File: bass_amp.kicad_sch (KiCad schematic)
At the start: 12 parts, among them Q1 BC547, Q2 BC547

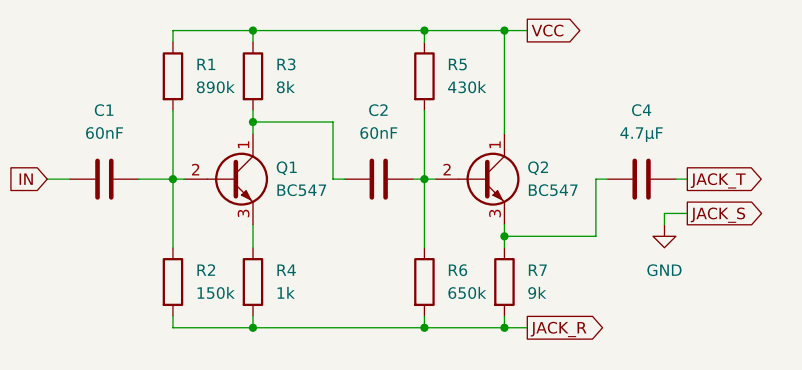
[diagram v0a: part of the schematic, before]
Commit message: Add a potentiometer to change the value of gain
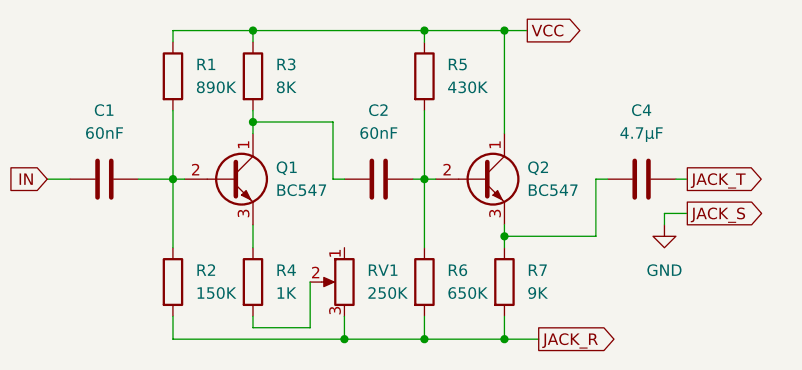
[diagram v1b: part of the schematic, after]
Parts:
- added RV1: 250K, symbol Device:R_Potentiometer
- R1: value 890k -> 890K
- R2: value 150k -> 150K
- R3: value 8k -> 8K
- R4: value 1k -> 1K
- R5: value 430k -> 430K
- R6: value 650k -> 650K
- R7: value 9k -> 9K
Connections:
- net JACK_R: now also RV1.3; no longer R4.2
- new net: R4.2, RV1.2
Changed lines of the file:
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@@
 	(paper "A4")
-	(junction
-		(at 106.68 91.44)
-		(diameter 0)
-		(color 0 0 0 0)
-	)
 	(junction
 		(at 78.74 58.42)
@@
 	)
 	(junction
-		(at 97.79 74.93)
+		(at 97.79 92.71)
 		(diameter 0)
 		(color 0 0 0 0)
 	)
 	(junction
-		(at 97.79 91.44)
+		(at 97.79 74.93)
 		(diameter 0)
 		(color 0 0 0 0)
@@
 	)
 	(junction
-		(at 69.85 74.93)
+		(at 106.68 92.71)
 		(diameter 0)
 		(color 0 0 0 0)
 	)
 	(junction
-		(at 78.74 91.44)
+		(at 69.85 74.93)
 		(diameter 0)
 		(color 0 0 0 0)
@@
 	)
 	(junction
+		(at 88.9 92.71)
+		(diameter 0)
+		(color 0 0 0 0)
+	)
+	(junction
 		(at 106.68 81.28)
 		(diameter 0)
@@
 	(wire
 		(pts
-			(xy 78.74 91.44) (xy 97.79 91.44)
-		)
-		(stroke
-			(width 0)
-			(type default)
-		)
-	)
-	(wire
-		(pts
-			(xy 106.68 90.17) (xy 106.68 91.44)
-		)
-		(stroke
-			(width 0)
-			(type default)
-		)
-	)
-	(wire
-		(pts
-			(xy 97.79 91.44) (xy 106.68 91.44)
+			(xy 85.09 86.36) (xy 85.09 91.44)
 		)
 		(stroke
@@
 	(wire
 		(pts
+			(xy 78.74 91.44) (xy 85.09 91.44)
+		)
+		(stroke
+			(width 0)
+			(type default)
+		)
+	)
+	(wire
+		(pts
 			(xy 127 78.74) (xy 124.46 78.74)
 		)
@@
 	(wire
 		(pts
-			(xy 69.85 91.44) (xy 78.74 91.44)
+			(xy 69.85 92.71) (xy 88.9 92.71)
 		)
 		(stroke
@@
 	(wire
 		(pts
+			(xy 97.79 92.71) (xy 106.68 92.71)
+		)
+		(stroke
+			(width 0)
+			(type default)
+		)
+	)
+	(wire
+		(pts
 			(xy 106.68 81.28) (xy 116.84 81.28)
 		)
@@
 	(wire
 		(pts
-			(xy 106.68 91.44) (xy 109.22 91.44)
+			(xy 78.74 90.17) (xy 78.74 91.44)
+		)
+		(stroke
+			(width 0)
+			(type default)
+		)
+	)
+	(wire
+		(pts
+			(xy 106.68 92.71) (xy 110.49 92.71)
 		)
 		(stroke
@@
 	(wire
 		(pts
-			(xy 78.74 90.17) (xy 78.74 91.44)
-		)
-		(stroke
-			(width 0)
-			(type default)
-		)
-	)
-	(wire
-		(pts
 			(xy 124.46 78.74) (xy 124.46 80.01)
 		)
@@
 	(wire
 		(pts
-			(xy 97.79 90.17) (xy 97.79 91.44)
-		)
-		(stroke
-			(width 0)
-			(type default)
-		)
-	)
-	(wire
-		(pts
 			(xy 97.79 59.69) (xy 97.79 58.42)
 		)
@@
 	(wire
 		(pts
+			(xy 88.9 92.71) (xy 97.79 92.71)
+		)
+		(stroke
+			(width 0)
+			(type default)
+		)
+	)
+	(wire
+		(pts
+			(xy 97.79 90.17) (xy 97.79 92.71)
+		)
+		(stroke
+			(width 0)
+			(type default)
+		)
+	)
+	(wire
+		(pts
 			(xy 97.79 67.31) (xy 97.79 74.93)
 		)
@@
 	(wire
 		(pts
-			(xy 69.85 90.17) (xy 69.85 91.44)
+			(xy 69.85 90.17) (xy 69.85 92.71)
 		)
 		(stroke
@@
 	(wire
 		(pts
+			(xy 106.68 90.17) (xy 106.68 92.71)
+		)
+		(stroke
+			(width 0)
+			(type default)
+		)
+	)
+	(wire
+		(pts
 			(xy 69.85 59.69) (xy 69.85 58.42)
+		)
+		(stroke
+			(width 0)
+			(type default)
+		)
+	)
+	(wire
+		(pts
+			(xy 88.9 90.17) (xy 88.9 92.71)
 		)
 		(stroke
@@
 	(global_label "JACK_R"
 		(shape output)
-		(at 109.22 91.44 0)
+		(at 110.49 92.71 0)
 		(fields_autoplaced yes)
 		(effects
@@
 		)
 		(property "Intersheetrefs" "${INTERSHEET_REFS}"
-			(at 119.039 91.44 0)
+			(at 120.309 92.71 0)
 			(effects
 				(font
@@
 			)
 		)
-		(property "Value" "430k"
+		(property "Value" "430K"
 			(at 100.33 64.7699 0)
 			(effects
@@
 			)
 		)
-		(property "Value" "150k"
+		(property "Value" "150K"
 			(at 72.39 87.6299 0)
 			(effects
@@
 				(path "/03e06cc7-32db-4918-be19-a630bf77c00d"
 					(reference "R2")
+					(unit 1)
+				)
+			)
+		)
+	)
+	(symbol
+		(lib_id "Device:R_Potentiometer")
+		(at 88.9 86.36 0)
+		(mirror y)
+		(unit 1)
+		(exclude_from_sim no)
+		(in_bom yes)
+		(on_board yes)
+		(dnp no)
+		(property "Reference" "RV1"
+			(at 91.44 85.0899 0)
+			(effects
+				(font
+					(size 1.27 1.27)
+				)
+				(justify right)
+			)
+		)
+		(property "Value" "250K"
+			(at 91.44 87.6299 0)
+			(effects
+				(font
+					(size 1.27 1.27)
+				)
+				(justify right)
+			)
+		)
+		(property "Footprint" ""
+			(at 88.9 86.36 0)
+			(effects
+				(font
+					(size 1.27 1.27)
+				)
+				(hide yes)
+			)
+		)
+		(property "Datasheet" "~"
+			(at 88.9 86.36 0)
+			(effects
+				(font
+					(size 1.27 1.27)
+				)
+				(hide yes)
+			)
+		)
+		(property "Description" "Potentiometer"
+			(at 88.9 86.36 0)
+			(effects
+				(font
+					(size 1.27 1.27)
+				)
+				(hide yes)
+			)
+		)
+		(pin "1"
+		)
+		(pin "3"
+		)
+		(pin "2"
+		)
+		(instances
+			(project ""
+				(path "/03e06cc7-32db-4918-be19-a630bf77c00d"
+					(reference "RV1")
 					(unit 1)
 				)
@@
 			)
 		)
-		(property "Value" "9k"
+		(property "Value" "9K"
 			(at 109.22 87.6299 0)
 			(effects
@@
 			)
 		)
-		(property "Value" "8k"
+		(property "Value" "8K"
 			(at 81.28 64.7699 0)
 			(effects
@@
 			)
 		)
-		(property "Value" "650k"
+		(property "Value" "650K"
 			(at 100.33 87.6299 0)
 			(effects
@@
 			)
 		)
-		(property "Value" "890k"
+		(property "Value" "890K"
 			(at 72.39 64.7699 0)
 			(effects
@@
 			)
 		)
-		(property "Value" "1k"
+		(property "Value" "1K"
 			(at 81.28 87.6299 0)
 			(effects

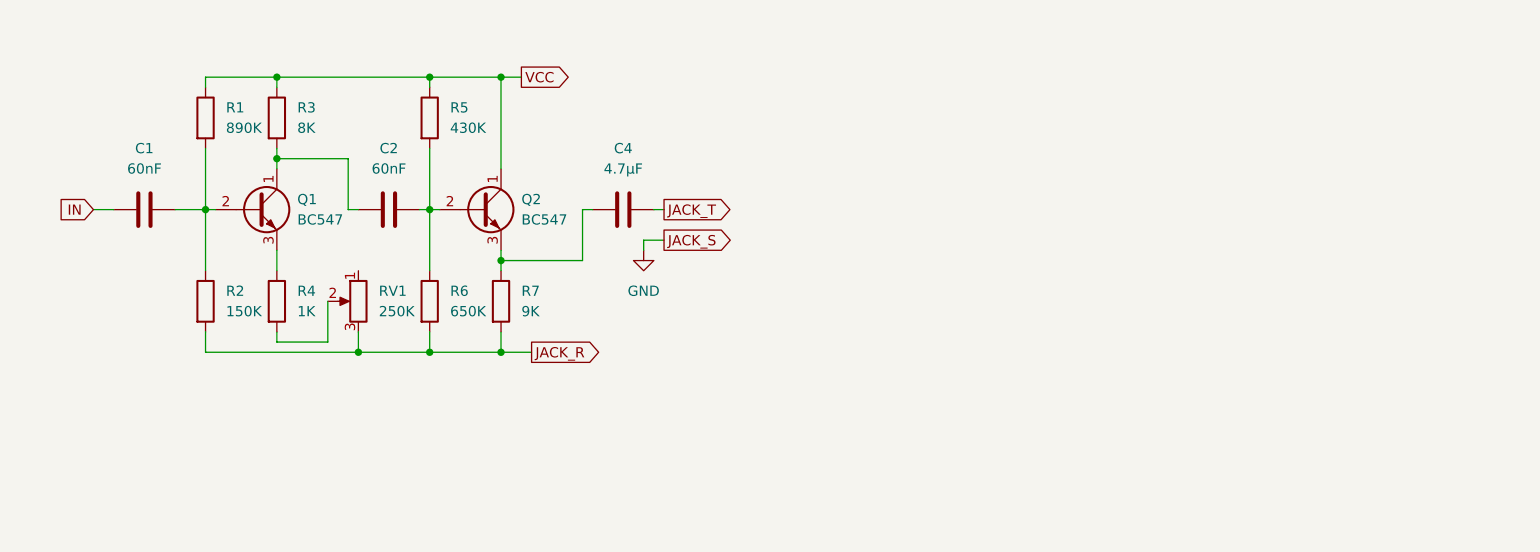
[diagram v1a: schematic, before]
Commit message: Add a bypass circuit
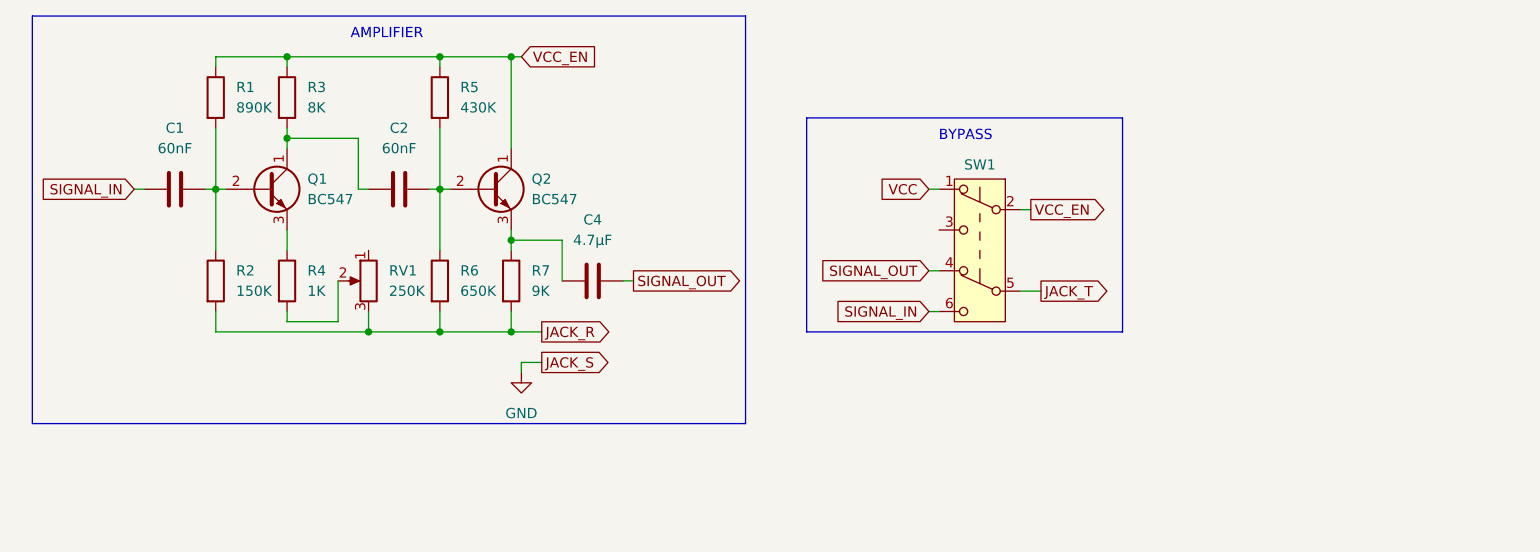
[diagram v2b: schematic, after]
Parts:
- added SW1: SW_Push_DPDT, symbol Switch:SW_Push_DPDT
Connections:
- net JACK_T: now also SW1.5 (B); no longer C4.1
- net VCC: now also SW1.1 (A); no longer Q2.1 (C), R1.1, R3.1, R5.1
- net IN renamed SIGNAL_IN
- net SIGNAL_IN: now also SW1.6 (C)
- new net SIGNAL_OUT: C4.1, SW1.4 (A)
- new net VCC_EN: Q2.1 (C), R1.1, R3.1, R5.1, SW1.2 (B)
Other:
- note added: "AMPLIFIER"
- note added: "BYPASS"
- moved on the sheet: C1, C2, C4, Q1, Q2, R1, R2, R3, R4, R5, R6, R7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

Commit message: Use standardized values for resistors and capacitors
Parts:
- C1, C2: value 60nF -> 62nF
- R1: value 890K -> 887k
- R2: value 150K -> 150k
- R3: value 8K -> 8.06k
- R4: value 1K -> 1k
- R5: value 430K -> 432k
- R6: value 650K -> 649k
- R7: value 9K -> 9.09k
- RV1: value 250K -> 250k
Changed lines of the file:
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@@
 			)
 		)
-		(property "Value" "430K"
+		(property "Value" "432k"
 			(at 101.6 62.2299 0)
 			(effects
@@
 			)
 		)
-		(property "Value" "150K"
+		(property "Value" "150k"
 			(at 73.66 85.0899 0)
 			(effects
@@
 			)
 		)
-		(property "Value" "250K"
+		(property "Value" "250k"
 			(at 92.71 85.0899 0)
 			(effects
@@
 			)
 		)
-		(property "Value" "9K"
+		(property "Value" "9.09k"
 			(at 110.49 85.0899 0)
 			(effects
@@
 			)
 		)
-		(property "Value" "8K"
+		(property "Value" "8.06k"
 			(at 82.55 62.2299 0)
 			(effects
@@
 			)
 		)
-		(property "Value" "650K"
+		(property "Value" "649k"
 			(at 101.6 85.0899 0)
 			(effects
@@
 			)
 		)
-		(property "Value" "890K"
+		(property "Value" "887k"
 			(at 73.66 62.2299 0)
 			(effects
@@
 			)
 		)
-		(property "Value" "60nF"
+		(property "Value" "62nF"
 			(at 93.98 67.31 90)
 			(effects
@@
 			)
 		)
-		(property "Value" "1K"
+		(property "Value" "1k"
 			(at 82.55 85.0899 0)
 			(effects
@@
 			)
 		)
-		(property "Value" "60nF"
+		(property "Value" "62nF"
 			(at 66.04 67.31 90)
 			(effects

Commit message: Add footprints for the elements
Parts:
- C1, C2: footprint (none) -> Capacitor_THT:C_Disc_D5.1mm_W3.2mm_P5.00mm
- C4: footprint (none) -> Capacitor_THT:C_Radial_D6.3mm_H7.0mm_P2.50mm
- R1, R2, R3, R4, R5, R6, R7: footprint (none) -> Resistor_THT:R_Axial_DIN0207_L6.3mm_D2.5mm_P7.62mm_Horizontal
- RV1: footprint (none) -> Custom_Connectors:Custom_Gain_Potentiometer
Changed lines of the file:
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@@
 			)
 		)
-		(property "Footprint" ""
+		(property "Footprint" "Resistor_THT:R_Axial_DIN0207_L6.3mm_D2.5mm_P7.62mm_Horizontal"
 			(at 97.282 60.96 90)
 			(effects
@@
 			)
 		)
-		(property "Footprint" ""
+		(property "Footprint" "Resistor_THT:R_Axial_DIN0207_L6.3mm_D2.5mm_P7.62mm_Horizontal"
 			(at 69.342 83.82 90)
 			(effects
@@
 			)
 		)
-		(property "Footprint" ""
+		(property "Footprint" "Custom_Connectors:Custom_Gain_Potentiometer"
 			(at 90.17 83.82 0)
 			(effects
@@
 			)
 		)
-		(property "Footprint" ""
+		(property "Footprint" "Resistor_THT:R_Axial_DIN0207_L6.3mm_D2.5mm_P7.62mm_Horizontal"
 			(at 106.172 83.82 90)
 			(effects
@@
 			)
 		)
-		(property "Footprint" ""
+		(property "Footprint" "Resistor_THT:R_Axial_DIN0207_L6.3mm_D2.5mm_P7.62mm_Horizontal"
 			(at 78.232 60.96 90)
 			(effects
@@
 			)
 		)
-		(property "Footprint" ""
+		(property "Footprint" "Resistor_THT:R_Axial_DIN0207_L6.3mm_D2.5mm_P7.62mm_Horizontal"
 			(at 97.282 83.82 90)
 			(effects
@@
 			)
 		)
-		(property "Footprint" ""
+		(property "Footprint" "Capacitor_THT:C_Radial_D6.3mm_H7.0mm_P2.50mm"
 			(at 114.3 84.7852 0)
 			(effects
@@
 			)
 		)
-		(property "Footprint" ""
+		(property "Footprint" "Resistor_THT:R_Axial_DIN0207_L6.3mm_D2.5mm_P7.62mm_Horizontal"
 			(at 69.342 60.96 90)
 			(effects
@@
 			)
 		)
-		(property "Footprint" ""
+		(property "Footprint" "Capacitor_THT:C_Disc_D5.1mm_W3.2mm_P5.00mm"
 			(at 90.17 73.3552 0)
 			(effects
@@
 			)
 		)
-		(property "Footprint" ""
+		(property "Footprint" "Resistor_THT:R_Axial_DIN0207_L6.3mm_D2.5mm_P7.62mm_Horizontal"
 			(at 78.232 83.82 90)
 			(effects
@@
 			)
 		)
-		(property "Footprint" ""
+		(property "Footprint" "Capacitor_THT:C_Disc_D5.1mm_W3.2mm_P5.00mm"
 			(at 62.23 73.3552 0)
 			(effects

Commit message: Add JACK output to the schematics
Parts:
- added J1: AudioJack3, symbol Connector_Audio:AudioJack3
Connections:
- net GND: now also J1.S
- net JACK_R: now also J1.R
- net JACK_T: now also J1.T
- net VCC renamed +9V
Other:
- note added: "JACK"
- moved on the sheet: SW1

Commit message: Add a footprint for the jack connector
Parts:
- J1: footprint (none) -> Custom_Connectors:Custom_Jack_TRS
- SW1: footprint (none) -> Button_Switch_THT:SW_CK_JS202011CQN_DPDT_Straight
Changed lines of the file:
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@@
 			)
 		)
-		(property "Footprint" ""
+		(property "Footprint" "Custom_Connectors:Custom_Jack_TRS"
 			(at 165.1 96.52 0)
 			(effects
@@
 			)
 		)
-		(property "Footprint" ""
+		(property "Footprint" "Button_Switch_THT:SW_CK_JS202011CQN_DPDT_Straight"
 			(at 162.56 64.77 0)
 			(effects

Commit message: Add power and signal sources to the schematics
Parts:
- added J2: SIGNAL, Connector_Wire:SolderWirePad_1x01_SMD_1x2mm, symbol Connector:Conn_01x01_Pin
- added J3: PWR, Connector_Wire:SolderWirePad_1x01_SMD_1x2mm, symbol Connector:Conn_01x01_Pin
- added J4: GND, Connector_Wire:SolderWirePad_1x01_SMD_1x2mm, symbol Connector:Conn_01x01_Pin
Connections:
- net +9V: now also J3.1 (Pin_1)
- net GND: now also J4.1 (Pin_1)
- net SIGNAL_IN: now also J2.1 (Pin_1)
- no-connect marks 0 -> 2
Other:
- note added: "POWER"
- note added: "SIGNAL IN"
- moved on the sheet: C1, C2, C4, J1, Q1, Q2, R1, R2, R3, R4, R5, R6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

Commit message: Rewire the pickups
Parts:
- added C3: 4.7μF, Capacitor_THT:C_Radial_D6.3mm_H7.0mm_P2.50mm, symbol Device:C
- added J3: PICKUP_GND, Connector_Wire:SolderWirePad_1x01_SMD_1x2mm, symbol Connector:Conn_01x01_Pin
- J2: value SIGNAL -> PICKUP_SIGNAL
- renumbered J3 to J4, J4 to J5
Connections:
- net JACK_R: now also C3.2, J3.1 (Pin_1)
- net at C4.2, Q2.3 (E), R7.1: now also C3.1
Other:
- note added: "PICKUPS"
- note removed: "SIGNAL IN"
- moved on the sheet: C4, J1, J2, J4, J5, SW1
